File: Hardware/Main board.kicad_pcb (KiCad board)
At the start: 4 copper layers, 16 parts, among them U3 LM66200DRLR, U4 MAX77827AEFD+T, U5 SC4215ASTRT

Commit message: PCB mid design
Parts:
- added 12VLED1: RED_LED, Resistor_SMD:R_0402_1005Metric, F.Cu at (115.3, 129.0)
- added 3V3LED1: BLUE_LED, Resistor_SMD:R_0402_1005Metric, F.Cu at (115.3, 131.0)
- added BOOTJUMPER1: Conn_01x02_Male, Connector_PinHeader_2.54mm:PinHeader_1x02_P2.54mm_Vertical, F.Cu at (106.3, 94.4)
- added C1: 10uF, Capacitor_SMD:C_0402_1005Metric, F.Cu at (125.5, 97.5)
- added C10: 0.1uF, Capacitor_SMD:C_0402_1005Metric, F.Cu at (134.3, 90.8)
- added C11: 0.1uF, Capacitor_SMD:C_0402_1005Metric, F.Cu at (135.2, 90.8)
- added C12: 100nF, Capacitor_SMD:C_0402_1005Metric, F.Cu at (130.6, 84.9)
- added C13: 11pF, Capacitor_SMD:C_0402_1005Metric, F.Cu at (118.7, 92.4)
- added C14: 11pF, Capacitor_SMD:C_0402_1005Metric, F.Cu at (120.6, 94.6)
- added C15: 100nF, Capacitor_SMD:C_0402_1005Metric, F.Cu at (135.6, 88.5)
- added C16: 10uF, Capacitor_SMD:C_0402_1005Metric, F.Cu at (134.6, 88.5)
- added C17: 47nF, Capacitor_SMD:C_0402_1005Metric, F.Cu at (147.5, 87.0)
- added C18: 100nF, Capacitor_SMD:C_0402_1005Metric, F.Cu at (125.8, 84.9)
- added C19: 100nF, Capacitor_SMD:C_0402_1005Metric, F.Cu at (135.7, 97.1)
- added C2: 1uF, Capacitor_SMD:C_0402_1005Metric, F.Cu at (122.2, 96.4)
- added C28: 0.1uF, Capacitor_SMD:C_0402_1005Metric, F.Cu at (158.9, 126.0)
- added C29: 0.1uF, Capacitor_SMD:C_0402_1005Metric, F.Cu at (158.9, 128.0)
- added C3: 0.1uF, Capacitor_SMD:C_0402_1005Metric, F.Cu at (112.5, 95.6)
- added C30: 0.1uF, Capacitor_SMD:C_0402_1005Metric, F.Cu at (132.7, 119.9)
- added C31: 1uF, Capacitor_SMD:C_0402_1005Metric, F.Cu at (139.0, 119.9)
- added C32: 0.1uF, Capacitor_SMD:C_0603_1608Metric, F.Cu at (135.6, 113.4)
- added C33: 0.1uF, Capacitor_SMD:C_0402_1005Metric, F.Cu at (141.0, 119.8)
- added C4: 1uF, Capacitor_SMD:C_0402_1005Metric, F.Cu at (125.5, 95.6)
- added C45: 10nF, Capacitor_SMD:C_0402_1005Metric, F.Cu at (154.8, 159.9)
- added C46: 22uF, Capacitor_SMD:C_0805_2012Metric, F.Cu at (150.2, 162.4)
- added C47: 82uF, Capacitor_SMD:CP_Elec_10x10.5, F.Cu at (143.7, 162.2)
- added C48: 15pF, Capacitor_SMD:C_0402_1005Metric, F.Cu at (161.7, 126.0)
- added C49: 1.2nf, Capacitor_SMD:C_0402_1005Metric, F.Cu at (161.7, 128.0)
- added C5: 0.1uF, Capacitor_SMD:C_0402_1005Metric, F.Cu at (125.5, 96.5)
- added C50: 4.7uF, Capacitor_SMD:C_0402_1005Metric, F.Cu at (158.8, 167.3)
- added C51: 0.1uF, Capacitor_SMD:C_0402_1005Metric, F.Cu at (160.3, 162.8)
- added C52: 0.1uF, Capacitor_SMD:C_0402_1005Metric, F.Cu at (160.3, 164.7)
- added C53: 180uF, Capacitor_Tantalum_SMD:CP_EIA-7260-20_AVX-M, F.Cu at (116.7, 163.9)
- added C54: 22uF, Capacitor_SMD:C_0805_2012Metric, F.Cu at (126.7, 161.9)
- added C6: 0.1uF, Capacitor_SMD:C_0402_1005Metric, F.Cu at (126.9, 95.0)
- added C7: 1uF, Capacitor_SMD:C_0402_1005Metric, F.Cu at (124.0, 93.2)
- added C8: 0.1uF, Capacitor_SMD:C_0402_1005Metric, F.Cu at (109.3, 95.4)
- added C9: 10nF, Capacitor_SMD:C_0402_1005Metric, F.Cu at (123.0, 93.2)
- added CRXLED1: ORANGE_LED, Resistor_SMD:R_0402_1005Metric, F.Cu at (115.3, 133.0)
- added CTXLED1: GREEN_LED, Resistor_SMD:R_0402_1005Metric, F.Cu at (115.3, 135.0)
- added D1: SM712_SOT23, Package_TO_SOT_SMD:SOT-23, F.Cu at (149.9, 87.3)
- added D2: SP0503BAHT, Package_TO_SOT_SMD:SOT-143, F.Cu at (123.6, 82.0)
- added D3: DST1550S, Package_TO_SOT_SMD:TO-277B, F.Cu at (110.2, 81.5)
- added D4: RED_LED, LED_SMD:LED_0603_1608Metric, F.Cu at (110.2, 88.5)
- added D5: 954-S-102T, Diode_SMD:D_1206_3216Metric, F.Cu at (112.5, 86.6)
- added D7: P6SMBJ28CA, Diode_SMD:D_SMA, F.Cu at (130.1, 122.3)
- added ENJUMPER1: Conn_01x02_Male, Connector_PinHeader_2.54mm:PinHeader_1x02_P2.54mm_Vertical, F.Cu at (115.2, 96.8)
- added Firing1: EMERALD_LED, LED_SMD:LED_0402_1005Metric, F.Cu at (119.3, 84.8)
- added H1: MountingHole_Pad, MountingHole:MountingHole_3.2mm_M3_DIN965_Pad, F.Cu at (94.9, 111.5)
- added H2: MountingHole_Pad, MountingHole:MountingHole_3.2mm_M3_DIN965_Pad, F.Cu at (94.9, 118.6)
- added H3: MountingHole_Pad, MountingHole:MountingHole_3.2mm_M3_DIN965_Pad, F.Cu at (94.9, 125.8)
- added H4: MountingHole_Pad, MountingHole:MountingHole_3.2mm_M3_DIN965_Pad, F.Cu at (94.9, 132.9)
- added J1: ST1W008S4TR2000, iclr:JAE_ST1W008S4TR2000, B.Cu at (80.8, 67.5)
- added J2: USB_C_Receptacle_USB2.0, Connector_USB:USB_C_Receptacle_Palconn_UTC16-G, F.Cu at (124.1, 76.7)
- added J3: Conn_01x02_Male, TerminalBlock_Phoenix:TerminalBlock_Phoenix_PT-1,5-2-3.5-H_1x02_P3.50mm_Horizontal, F.Cu at (101.6, 76.1)
- added J4: USB_C_Receptacle_USB2.0, Connector_USB:USB_C_Receptacle_Palconn_UTC16-G, F.Cu at (134.7, 76.7)
- added JP1: TermJP, Jumper:SolderJumper-2_P1.3mm_Open_RoundedPad1.0x1.5mm, F.Cu at (145.3, 87.4)
- added L1: 2.0nH, Inductor_SMD:L_0402_1005Metric, F.Cu at (125.5, 94.6)
- added L2: 20nH, Inductor_SMD:L_0402_1005Metric, F.Cu at (123.6, 91.8)
- added L5: 4.7uH, Inductor_SMD:L_10.4x10.4_H4.8, F.Cu at (166.7, 163.9)
- added Q1: BUK9M11-40EX, Package_TO_SOT_SMD:LFPAK33, F.Cu at (114.4, 82.3)
- added Q2: BSZ025N04LS, iclr:BSZ025N04LS, F.Cu at (133.6, 116.3)
- added Q3: BSZ025N04LS, iclr:BSZ025N04LS, F.Cu at (138.2, 116.3)
- added Q4: BUK9M11-40EX, Package_TO_SOT_SMD:LFPAK33, F.Cu at (159.9, 155.7)
- added Q5: BUK9M11-40EX, Package_TO_SOT_SMD:LFPAK33, F.Cu at (164.7, 155.7)
- added R1: 10K, Resistor_SMD:R_0402_1005Metric, F.Cu at (122.2, 98.7)
- added R10: 60, Resistor_SMD:R_0603_1608Metric, F.Cu at (145.1, 89.5)
- added R11: 5.1k, Resistor_SMD:R_0402_1005Metric, F.Cu at (126.1, 81.3)
- added R12: 5.1k, Resistor_SMD:R_0402_1005Metric, F.Cu at (119.9, 80.7)
- added R13: 5.1k, Resistor_SMD:R_0402_1005Metric, F.Cu at (127.1, 81.3)
- added R18: 1k, Resistor_SMD:R_0402_1005Metric, F.Cu at (121.1, 131.0)
- added R19: 120, Resistor_SMD:R_0402_1005Metric, F.Cu at (117.4, 84.8)
- added R2: 470, Resistor_SMD:R_0402_1005Metric, F.Cu at (98.5, 73.3)
- added R20: 120, Resistor_SMD:R_0603_1608Metric, F.Cu at (113.2, 88.5)
- added R21: 10k, Resistor_SMD:R_0402_1005Metric, F.Cu at (134.1, 92.9)
- added R22: 10k, Resistor_SMD:R_0402_1005Metric, F.Cu at (134.1, 95.3)
- added R23: 5.1k, Resistor_SMD:R_0402_1005Metric, F.Cu at (136.5, 80.8)
- added R24: 5.1k, Resistor_SMD:R_0402_1005Metric, F.Cu at (133.0, 81.3)
- added R25: 5.1k, Resistor_SMD:R_0402_1005Metric, F.Cu at (132.0, 81.3)
- added R26: 2m, Resistor_SMD:R_2512_6332Metric_Pad1.40x3.35mm_HandSolder, F.Cu at (183.7, 126.0)
- added R27: 10, Resistor_SMD:R_0402_1005Metric, F.Cu at (148.0, 128.5)
- added R28: 10, Resistor_SMD:R_0402_1005Metric, F.Cu at (148.0, 130.5)
- added R29: 3.3k, Resistor_SMD:R_0402_1005Metric, F.Cu at (148.0, 132.5)
- added R3: 10K, Resistor_SMD:R_0402_1005Metric, F.Cu at (118.7, 99.4)
- added R30: 3.3k, Resistor_SMD:R_0402_1005Metric, F.Cu at (148.0, 134.5)
- added R31: 10k, Resistor_SMD:R_0402_1005Metric, F.Cu at (134.9, 122.9)
- added R32: 100k, Resistor_SMD:R_0402_1005Metric, F.Cu at (132.8, 121.8)
- added R33: 5.1k, Resistor_SMD:R_0402_1005Metric, F.Cu at (132.8, 123.7)
- added R34: 4.22k, Resistor_SMD:R_0402_1005Metric, F.Cu at (132.7, 125.6)
- added R35: 10k, Resistor_SMD:R_0402_1005Metric, F.Cu at (80.1, 76.3)
- added R4: 470, Resistor_SMD:R_0402_1005Metric, F.Cu at (118.2, 135.0)
- added R42: 10k, Resistor_SMD:R_0402_1005Metric, F.Cu at (138.0, 97.0)
- added R44: 178k, Resistor_SMD:R_0402_1005Metric, F.Cu at (123.0, 156.5)
- added R45: 10, Resistor_SMD:R_0402_1005Metric, F.Cu at (162.3, 154.5)
- added R46: 10, Resistor_SMD:R_0402_1005Metric, F.Cu at (158.5, 158.9)
- added R47: 100k, Resistor_SMD:R_0402_1005Metric, F.Cu at (123.0, 162.5)
- added R48: 50k, Resistor_SMD:R_0402_1005Metric, F.Cu at (152.9, 161.7)
- added R49: 10m, Resistor_SMD:R_0402_1005Metric, F.Cu at (152.8, 165.5)
- added R5: 1k, Resistor_SMD:R_0402_1005Metric, F.Cu at (118.2, 137.0)
- added R50: 6.19k, Resistor_SMD:R_0402_1005Metric, F.Cu at (156.0, 167.8)
- added R51: 31.6k, Resistor_SMD:R_0402_1005Metric, F.Cu at (157.0, 167.8)
- added R52: 160k, Resistor_SMD:R_0402_1005Metric, F.Cu at (153.8, 136.5)
- added R6: 499R, Resistor_SMD:R_0402_1005Metric, F.Cu at (98.5, 77.1)
- added R7: 3k, Resistor_SMD:R_0402_1005Metric, F.Cu at (121.1, 129.0)
- added R8: 0, Resistor_SMD:R_0603_1608Metric, F.Cu at (142.5, 83.9)
- added R9: 60, Resistor_SMD:R_0603_1608Metric, F.Cu at (145.1, 85.4)
- added TP1: TestPoint, TestPoint:TestPoint_Pad_D1.0mm, F.Cu at (115.9, 73.5)
- added TP10: TestPoint, TestPoint:TestPoint_Pad_D1.0mm, F.Cu at (95.4, 76.7)
- added TP11: TestPoint, TestPoint:TestPoint_Pad_D1.0mm, F.Cu at (172.5, 124.8)
- added TP12: TestPoint, TestPoint:TestPoint_Pad_D1.0mm, F.Cu at (172.5, 127.8)
- added TP2: TestPoint, TestPoint:TestPoint_Pad_D1.0mm, F.Cu at (115.9, 76.0)
- added TP3: TestPoint, TestPoint:TestPoint_Pad_D1.0mm, F.Cu at (148.5, 79.4)
- added TP4: TestPoint, TestPoint:TestPoint_Pad_D1.5mm, F.Cu at (102.1, 109.8)
- added TP5: TestPoint, TestPoint:TestPoint_Pad_D1.5mm, F.Cu at (102.1, 113.3)
- added TP6: TestPoint, TestPoint:TestPoint_Pad_D1.5mm, F.Cu at (102.1, 116.9)
- added TP7: TestPoint, TestPoint:TestPoint_Pad_D1.0mm, F.Cu at (146.1, 79.5)
- added TP8: TestPoint, TestPoint:TestPoint_Pad_D1.5mm, F.Cu at (102.1, 120.4)
- added TP9: TestPoint, TestPoint:TestPoint_Pad_D1.0mm, F.Cu at (95.4, 73.7)
- added TXLED1: GREEN_LED, Resistor_SMD:R_0402_1005Metric, F.Cu at (98.5, 75.2)
- added U1: ESP32-S3, iclr:QFN40P700X700X90-57N, F.Cu at (128.7, 90.0)
- added U10: TPS55288QRPMRQ1, iclr:TPS552882QRPMRQ1, F.Cu at (156.8, 163.7)
- added U11: DPS368, iclr:XDCR_DPS310, F.Cu at (128.2, 84.6)
- added U12: TCMT1109, Package_SO:SOP-4_4.4x2.6mm_P1.27mm, F.Cu at (119.0, 86.8)
- added U2: SN65HVD230, Package_SO:SOIC-8_3.9x4.9mm_P1.27mm, F.Cu at (139.9, 87.4)
- added U7: BU27006MUC-ZTR, iclr:BU27006MUCZTR, F.Cu at (137.2, 94.2)
- added U8: INA219AxDCN, Package_TO_SOT_SMD:SOT-23-8, F.Cu at (183.1, 121.0)
- added U9: LM74810, iclr:SON50P300X300X80-13N-D, F.Cu at (135.9, 120.6)
- added USBLED1: WHITE_LED, Resistor_SMD:R_0402_1005Metric, F.Cu at (128.1, 81.3)
- added USBLED2: WHITE_LED, Resistor_SMD:R_0402_1005Metric, F.Cu at (131.0, 81.3)
- added Y1: R940000171, Crystal:Crystal_SMD_2016-4Pin_2.0x1.6mm, F.Cu at (120.5, 92.7)
- C23: footprint Capacitor_SMD:C_0603_1608Metric -> Capacitor_SMD:C_0805_2012Metric
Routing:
- net /BOOT: track 0.00 -> 44.6 mm
- net GND: track 7.31 -> 49.2 mm, vias 8 -> 34
- net /CAN-: track 0.00 -> 39.3 mm
- net /CAN+: track 0.00 -> 30.4 mm
- net +3V3: track 1.61 -> 30.5 mm, vias 1 -> 11
- net /Voltage Regulation/Switch_out: track 0.00 -> 22.8 mm
- net Net-(J3-Pin_2): track 0.00 -> 22.3 mm, vias 0 -> 3
- net /CHIP_PU: track 0.00 -> 21.3 mm
- net /Data+: track 0.00 -> 19.6 mm
- net /Data-: track 0.00 -> 19.4 mm
- net Net-(Q4-D): track 0.00 -> 19.0 mm
- net AGND: track 0.00 -> 17.9 mm, vias 0 -> 7
- net /Voltage Regulation/VOUT_2: track 0.00 -> 16.9 mm
- net /Interrupt : track 0.00 -> 15.3 mm
- net /Voltage Regulation/C: track 0.00 -> 14.8 mm
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- added copper zone on F.Cu, net /Voltage Regulation/C
- added copper zone on F.Cu, net /Voltage Regulation/Switch_out
- added copper zone on F.Cu, net /Voltage Regulation/VIN
- added copper zone on F.Cu, net AGND
- removed copper zone on F.Cu, net GND

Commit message: PCB done more ish
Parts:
- C47: footprint Capacitor_SMD:CP_Elec_10x10.5 -> Capacitor_Tantalum_SMD:CP_EIA-6032-28_Kemet-C
- R35: moved to B.Cu
- moved R26 103.0 mm to (84.6, 98.1), turned to 180 degrees
- moved U8 101.0 mm to (83.5, 104.4), turned to -90 degrees
- moved C51 98.8 mm to (94.6, 89.0)
- moved R50 98.2 mm to (89.7, 95.4)
- moved R51 98.2 mm to (90.7, 95.4)
- moved C45 97.9 mm to (89.0, 87.5), turned to 0 degrees
- moved U10 97.8 mm to (91.1, 91.3)
- moved C52 97.8 mm to (94.6, 92.2)
- moved C50 97.6 mm to (92.8, 95.4), turned to 90 degrees
- moved R48 97.4 mm to (87.6, 89.4), turned to 90 degrees
- moved L5 97.0 mm to (101.0, 92.6), turned to 180 degrees
- moved R49 96.8 mm to (86.6, 94.8), turned to -90 degrees
- moved C46 96.0 mm to (85.8, 91.2)
- moved R46 95.2 mm to (100.6, 83.3), turned to 180 degrees
- moved C47 94.4 mm to (82.8, 90.1)
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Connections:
- R47 pad 2: GND -> AGND
- U1 pad 13: /VSPI_MOSI -> /SD1_CS
- U1 pad 14: /SD1_CS -> /VSPI_MOSI
- U1 pad 48: /CC -> unconnected-(U1-MTMS/JTAG/GPIO42-Pad48)
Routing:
- net /INT: track 0.00 -> 83.9 mm, vias 0 -> 3
- net /SD1_DET: track 3.03 -> 81.2 mm, vias 0 -> 2
- net /SCL_I2C: track 5.67 -> 75.4 mm, vias 0 -> 4
- net /SDA-BuckBC: track 0.00 -> 57.3 mm, vias 0 -> 4
- net /VSPI_MISO: track 2.28 -> 53.0 mm, vias 0 -> 1
- net /SDA-CS: track 11.4 -> 61.9 mm, vias 0 -> 3
- net /SD1_CS: track 0.00 -> 48.5 mm, vias 0 -> 1
- net /VSPI_MOSI: track 0.00 -> 48.0 mm, vias 0 -> 1
- net /VSPI_SCLK: track 0.00 -> 47.7 mm, vias 0 -> 2
- net /BOOT: track 44.6 -> 4.32 mm
- net /Cont 1: track 11.6 -> 39.5 mm, vias 0 -> 2
- net /Voltage Regulation/Switch_out: track 22.8 -> 50.6 mm, vias 0 -> 10
- net /Nuke 1: track 11.8 -> 37.5 mm, vias 0 -> 2
- net /BUS_VMON: track 5.22 -> 27.5 mm, vias 0 -> 2
- net Net-(J3-Pin_2): track 22.3 -> 0.00 mm, vias 3 -> 0
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- added copper zone on F.Cu, net /BOOT
- added copper zone on F.Cu, net /CAN_RX
- added copper zone on F.Cu, net /CAN_TX
- added copper zone on F.Cu, net /CHIP_PU
- added copper zone on F.Cu, net /PyroPWR
- added copper zone on F.Cu, net /SCL_I2C
- added copper zone on F.Cu, net /SDA-CS
- added copper zone on F.Cu, net /Voltage Regulation/DGate
- added copper zone on F.Cu, net /Voltage Regulation/DITH/SYNC_2
- added copper zone on F.Cu, net /Voltage Regulation/DR1L_2
- added copper zone on F.Cu, net /Voltage Regulation/HGate
- added copper zone on F.Cu, net /Voltage Regulation/ISN_2
- added copper zone on F.Cu, net /Voltage Regulation/SHNT_IN+
- added copper zone on F.Cu, net /Voltage Regulation/SHNT_IN-
- added copper zone on F.Cu, net /Voltage Regulation/SW2_2
- added copper zone on F.Cu, net /Voltage Regulation/VCC_2
- added copper zone on F.Cu, net /Voltage Regulation/VOUT_2
- added copper zone on B.Cu, net AGND
- added copper zone on F.Cu, net GND
- added copper zone on F.Cu, net Net-(C14-Pad1)
- added copper zone on F.Cu, net Net-(D3-K)
- added copper zone on F.Cu, net Net-(J3-Pin_2)
- added copper zone on F.Cu, net Net-(JP1-B)
- added copper zone on F.Cu, net Net-(Q4-D)
- added copper zone on F.Cu, net Net-(Q4-G)
- added copper zone on F.Cu, net Net-(Q5-G)
- added copper zone on F.Cu, net Net-(U1-XTAL_N)
- added copper zone on F.Cu, net Net-(U10-COMP)
- added copper zone on F.Cu, net Net-(U10-EN/UVLO)
- added copper zone on F.Cu, net Net-(U9-OV)

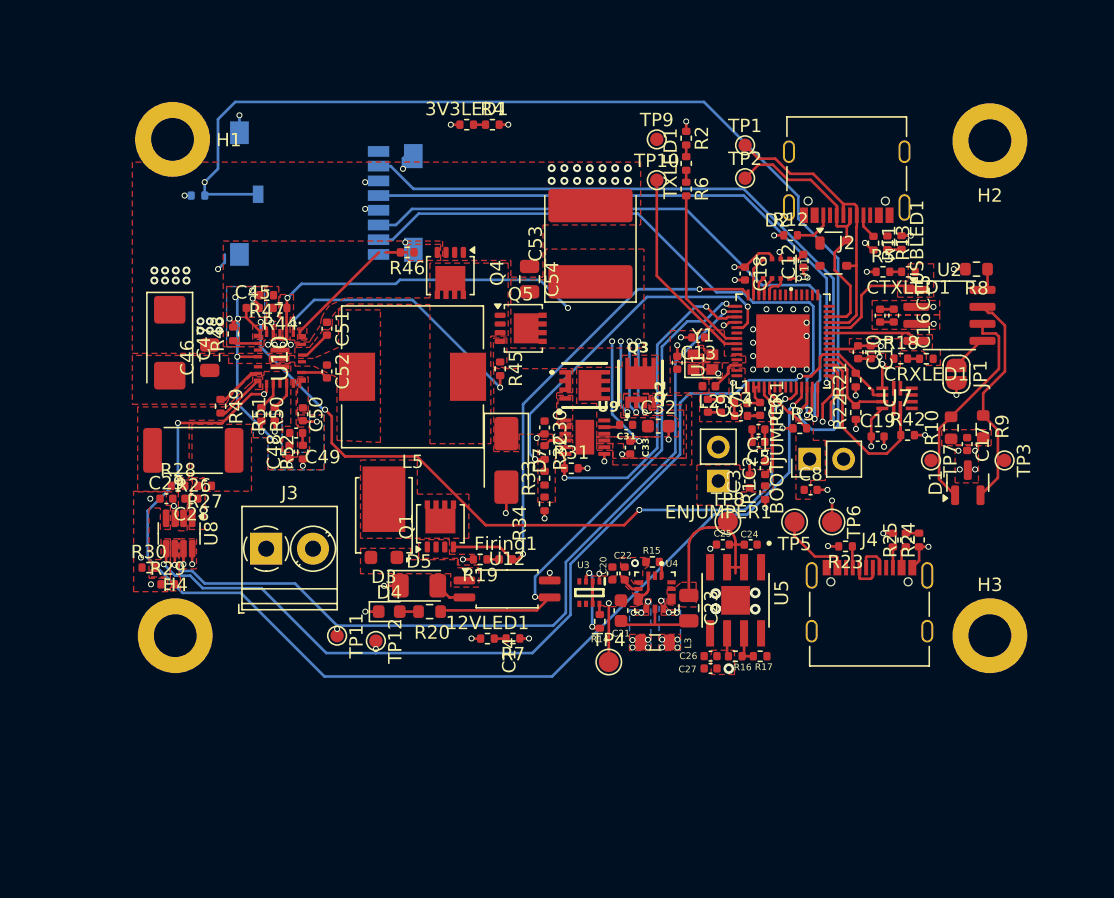
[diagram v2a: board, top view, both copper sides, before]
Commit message: Crosshair V1.0
New pyro connectors, silkscreen sorted, mostly connected properly + cool new name and image
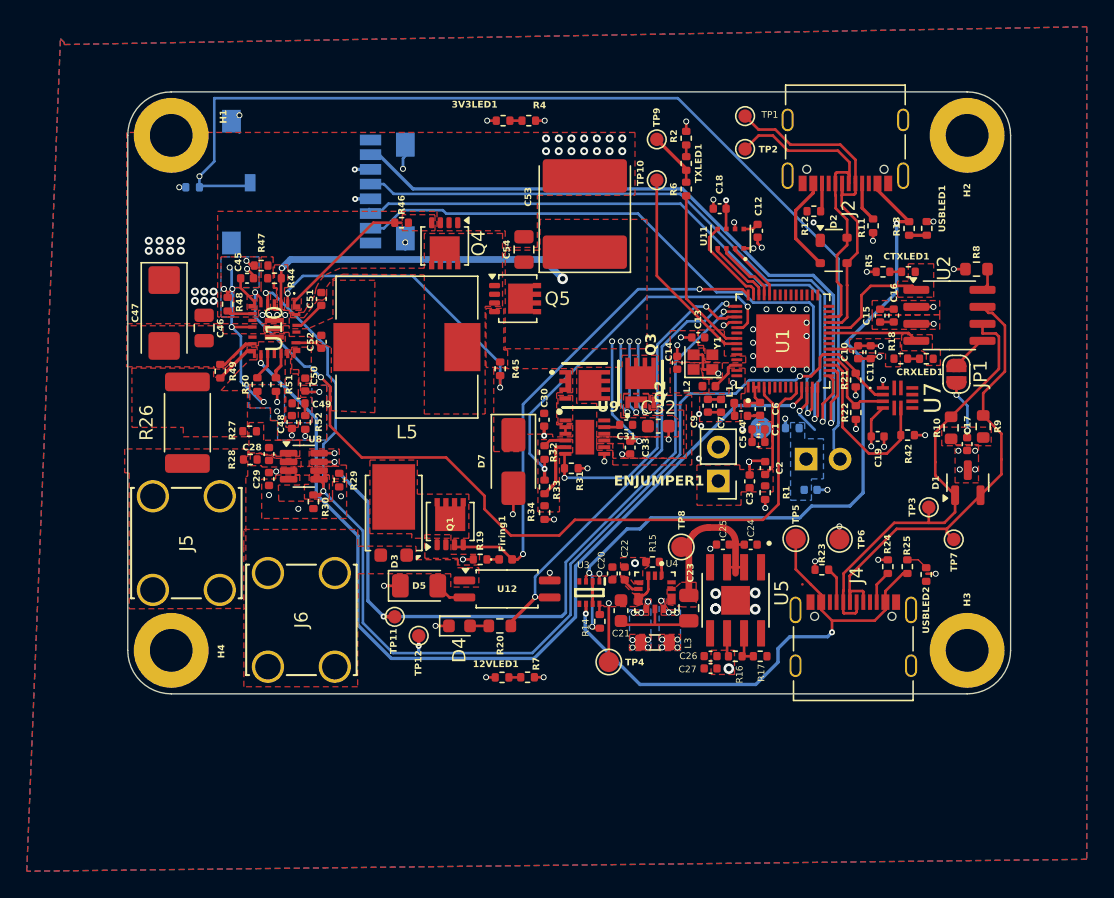
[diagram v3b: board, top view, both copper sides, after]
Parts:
- removed J3: Conn_01x02_Male, TerminalBlock_Phoenix:TerminalBlock_Phoenix_PT-1,5-2-3.5-H_1x02_P3.50mm_Horizontal
- added G***: LOGO, LOGO, F.Cu at (131.4, 68.0)
- added J5: 7788, iclr:CONN_7788_KEY, F.Cu at (81.6, 108.6)
- added J6: 7788, iclr:CONN_7788_KEY, F.Cu at (90.2, 114.3)
- BOOTJUMPER1, C8, R3: moved to B.Cu
- J2, J4: footprint Connector_USB:USB_C_Receptacle_Palconn_UTC16-G -> iclr:USB_C_Receptacle_Palconn_UTC16-G
- moved R29 15.0 mm to (95.5, 100.4), turned to 90 degrees
- moved R30 13.2 mm to (93.6, 102.0), turned to 90 degrees
- moved U8 10.6 mm to (92.8, 99.3), turned to 0 degrees
- moved C29 7.81 mm to (90.2, 100.3), turned to 90 degrees
- moved C28 6.69 mm to (90.2, 98.4), turned to -90 degrees
- moved TP3 6.66 mm to (139.6, 102.4)
- moved TP7 6.15 mm to (141.4, 104.8)
- moved R28 5.75 mm to (88.8, 98.8)
- moved D4 5.36 mm to (104.5, 111.3)
- moved R20 5.36 mm to (107.5, 111.3)
- moved R27 5.29 mm to (88.8, 96.7), turned to 0 degrees
- moved C18 5.21 mm to (123.9, 80.1), turned to 180 degrees
- moved TP11 4.53 mm to (99.6, 110.6)
- moved C12 4.09 mm to (126.8, 81.7)
- moved U11 4.09 mm to (124.8, 82.3)
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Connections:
- R26 pad 1: /PyroPWR -> /Voltage Regulation/ISN_2
- R26 pad 2: /Voltage Regulation/ISN_2 -> /PyroPWR
- R27 pad 1: /PyroPWR -> /Voltage Regulation/ISN_2
- R28 pad 1: /Voltage Regulation/ISN_2 -> /PyroPWR
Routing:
- net VBUS: track 5.51 -> 63.2 mm, vias 2 -> 3
- net RBUS_uC_V: track 7.39 -> 40.3 mm, vias 0 -> 2
- net /CAN+: track 19.1 -> 34.7 mm
- net /INT: track 83.9 -> 68.5 mm, vias 3 -> 2
- net /CAN-: track 18.9 -> 33.9 mm
- net /SCL_I2C: track 75.4 -> 88.4 mm
- net /SDA-CS: track 61.9 -> 55.0 mm, vias 3 -> 2
- net /Cont 1: track 39.5 -> 33.8 mm
- net Net-(U9-OV): track 0.00 -> 4.51 mm
- net /SDA-BuckBC: track 57.3 -> 61.6 mm, vias 4 -> 2
- net GND: track 51.8 -> 47.5 mm, vias 99 -> 102
- net /Data+: track 20.9 -> 24.8 mm
- net /BOOT: track 4.32 -> 0.46 mm
- net /MISO: track 2.99 -> 6.78 mm
- net /SCK_Baro: track 1.37 -> 4.97 mm
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- added copper zone on In2.Cu, net +3V3
- added copper zone on B.Cu, net /BOOT
- added copper zone on B.Cu, net GND
- added copper zone on In1.Cu, net GND
- removed copper zone on F.Cu, net /BOOT
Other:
- board outline added: 66 x 45 mm
- board text added: "CROSSHAIR V1.0"
- board text added: "Designed by William Richards Electronics 2025"

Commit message: SD card fix + logos
Changed SD card from the lock in to the push in
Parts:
- added G***: LOGO, iclr:rae_logo_6mm, F.Cu at (90.7, 76.7)
- added G***: LOGO, iclr:iclr_logo_estd2018_6mm, F.Cu at (97.7, 76.7)
- added G***: LOGO, iclr:rae_logo_6mm, B.Cu at (86.4, 89.6)
- added G***: LOGO, iclr:iclr_logo_estd2018_6mm, B.Cu at (86.4, 96.6)
- J1: footprint iclr:JAE_ST1W008S4TR2000 -> Connector_Card:microSD_HC_Hirose_DM3AT-SF-PEJM5
- moved R35 44.3 mm to (128.6, 82.3), turned to -90 degrees
- moved J1 18.5 mm to (112.5, 79.8), turned to 0 degrees
- moved C53 2.26 mm to (114.6, 82.6)
- moved Q5 2.17 mm to (108.6, 89.0)
- moved G*** 1.87 mm to (130.3, 69.5)
- moved Q4 1.70 mm to (103.8, 84.3)
- moved R46 1.70 mm to (100.6, 82.8)
- moved L5 1.67 mm to (100.5, 92.1)
- moved C54 0.90 mm to (108.9, 83.9)
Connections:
- R35 pad 2: /SD1_DET -> /SD_DET
- U1 pad 12: /SD1_DET -> /SD_DET
- U1 pad 13: /SD1_CS -> /SD_DAT3
- U1 pad 14: /VSPI_MOSI -> /SD_CLK
- U1 pad 15: /VSPI_SCLK -> /SD_DAT0
- U1 pad 16: /VSPI_MISO -> /SD_DAT1
- U1 pad 36: unconnected-(U1-SPICLK_N/GPIO48-Pad36) -> /SD_CMD
- U1 pad 37: unconnected-(U1-SPICLK_P/GPIO47-Pad37) -> /SD_DAT2
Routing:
- net /SD1_DET: track 81.0 -> 0.00 mm, vias 2 -> 0
- net /VSPI_MISO: track 53.2 -> 0.00 mm, vias 1 -> 0
- net /VSPI_SCLK: track 51.3 -> 0.00 mm, vias 1 -> 0
- net /SD_DET: track 0.00 -> 49.5 mm, vias 0 -> 1
- net /VSPI_MOSI: track 48.6 -> 0.00 mm, vias 1 -> 0
- net /SD1_CS: track 46.9 -> 0.00 mm, vias 1 -> 0
- net /SD_DAT1: track 0.00 -> 41.8 mm, vias 0 -> 1
- net /SD_DAT0: track 0.00 -> 39.1 mm, vias 0 -> 1
- net /SD_CLK: track 0.00 -> 34.7 mm, vias 0 -> 1
- net /SD_DAT3: track 0.00 -> 29.1 mm, vias 0 -> 1
- net /SD_CMD: track 0.00 -> 19.5 mm, vias 0 -> 1
- net /SD_DAT2: track 0.00 -> 14.7 mm, vias 0 -> 1
- net GND: track 47.5 -> 50.2 mm
- net Net-(U10-DR1H): track 22.7 -> 21.2 mm
- net VBUS: track 63.2 -> 61.9 mm
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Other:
- board text added: "C46"
